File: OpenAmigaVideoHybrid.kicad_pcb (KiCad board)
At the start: 2 copper layers, 56.4 x 21.1 mm, 52 parts, among them J1 Conn_01x22, J99 OSHW_LOGO, Q1 2N3904, Q2 2N3904, Q3 2N3904, Q4 2N3904, Q5 2N3904, Q6 2N3906

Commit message: work in progress
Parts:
- removed J99: OSHW_LOGO, w_logo:Logo_copper_OSHW_6x6mm
- added C6: 100n, Capacitor_SMD:C_0603_1608Metric, F.Cu at (102.9, 91.9)
- added JP1: VCC_VID_BRIDGE, Jumper:SolderJumper-2_P1.3mm_Open_RoundedPad1.0x1.5mm, F.Cu at (162.8, 94.0)
- added R40: 2k, Resistor_SMD:R_0603_1608Metric, F.Cu at (151.8, 95.0)
- added R41: 2k, Resistor_SMD:R_0603_1608Metric, F.Cu at (139.1, 95.0)
- added R42: 2k, Resistor_SMD:R_0603_1608Metric, F.Cu at (126.4, 95.0)
- added R43: 4k7, Resistor_SMD:R_0603_1608Metric, F.Cu at (123.8, 95.0)
- added R44: 4k7, Resistor_SMD:R_0603_1608Metric, F.Cu at (136.5, 95.0)
- added R45: 4k7, Resistor_SMD:R_0603_1608Metric, F.Cu at (149.2, 95.0)
- added R46: 1k5, Resistor_SMD:R_0603_1608Metric, F.Cu at (129.8, 91.9)
- added R47: 1k5, Resistor_SMD:R_0603_1608Metric, F.Cu at (118.0, 95.0)
- added R48: 470, Resistor_SMD:R_0603_1608Metric, F.Cu at (142.4, 91.9)
- added R49: 3k3, Resistor_SMD:R_0603_1608Metric, F.Cu at (155.1, 91.9)
- added R50: 4k7, Resistor_SMD:R_0603_1608Metric, F.Cu at (119.6, 95.0)
- C1, C2, C3, C4: footprint Capacitors_SMD:C_0805_HandSoldering -> Capacitor_SMD:C_0603_1608Metric; moved to F.Cu
- C5: footprint Capacitors_SMD:C_0805_HandSoldering -> Capacitor_SMD:C_0603_1608Metric
- J1: footprint OpenAmigaVideoHybrid:Pin_Header_Straight_1x22_Pitch2.54mm -> Connector_PinHeader_2.54mm:PinHeader_1x22_P2.54mm_Vertical; moved to F.Cu
- Q1, Q2, Q3, Q4: value 2N3904 -> MMBT3904; footprint OpenAmigaVideoHybrid:2N3904_2N3906_SOT-23 -> Package_TO_SOT_SMD:SOT-23; moved to F.Cu
- Q5: value 2N3904 -> MMBT3904; footprint OpenAmigaVideoHybrid:2N3904_2N3906_SOT-23 -> Package_TO_SOT_SMD:SOT-23
- Q6: value 2N3906 -> S9012; footprint OpenAmigaVideoHybrid:2N3904_2N3906_SOT-23 -> Package_TO_SOT_SMD:SOT-23
- R1, R10, R13, R14, R15, R16, R17, R18, R2, R21, R22, R23, R24, R25, R26, R27, R28, R29, R5, R6, R7, R8, R9: footprint Resistors_SMD:R_0805_HandSoldering -> Resistor_SMD:R_0603_1608Metric; moved to F.Cu
- R11, R19, R3: value 4k -> 2k; footprint Resistors_SMD:R_0805_HandSoldering -> Resistor_SMD:R_0603_1608Metric; moved to F.Cu
- R12, R20, R4: value 8k -> 3k3; footprint Resistors_SMD:R_0805_HandSoldering -> Resistor_SMD:R_0603_1608Metric; moved to F.Cu
- R30: value 90.9k -> 91k; footprint Resistors_SMD:R_0805_HandSoldering -> Resistor_SMD:R_0603_1608Metric
- R31, R34: value 37.4k -> 36k; footprint Resistors_SMD:R_0805_HandSoldering -> Resistor_SMD:R_0603_1608Metric
- R32: value 13.3k -> 10k; footprint Resistors_SMD:R_0805_HandSoldering -> Resistor_SMD:R_0603_1608Metric
- R33: value 6.04k -> 5k6; footprint Resistors_SMD:R_0805_HandSoldering -> Resistor_SMD:R_0603_1608Metric
- R35: value 19.6k -> 15k; footprint Resistors_SMD:R_0805_HandSoldering -> Resistor_SMD:R_0603_1608Metric
- R36: value 220 -> 270; footprint Resistors_SMD:R_0805_HandSoldering -> Resistor_SMD:R_0603_1608Metric
- R37, R38: value 36 -> 33; footprint Resistors_SMD:R_0805_HandSoldering -> Resistor_SMD:R_0603_1608Metric
- R39: footprint Resistors_SMD:R_0805_HandSoldering -> Resistor_SMD:R_0603_1608Metric
- moved R27 64.2 mm to (104.9, 95.1), turned to -90 degrees
- moved Q4 63.7 mm to (107.8, 91.4), turned to 90 degrees
- moved C4 63.7 mm to (102.9, 95.0), turned to 90 degrees
- moved R28 62.2 mm to (107.4, 95.0)
- moved R25 61.1 mm to (104.9, 91.9)
- moved R29 60.9 mm to (110.2, 98.0)
- moved Q6 59.8 mm to (113.3, 91.4)
- moved R39 58.6 mm to (112.0, 98.0), turned to 90 degrees
- moved C5 56.3 mm to (112.0, 95.0)
- moved R37 55.4 mm to (114.3, 95.0), turned to 90 degrees
- moved R38 54.8 mm to (116.1, 95.0), turned to -90 degrees
- moved R26 52.4 mm to (114.3, 98.0)
- moved R36 51.1 mm to (113.2, 88.6), turned to 0 degrees
- moved Q5 49.4 mm to (117.0, 91.4), turned to -90 degrees
- moved R31 49.0 mm to (118.0, 98.0)
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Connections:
- J1 pad 2: VCC -> VID
- Q1 pad 1: Net-(Q1-Pad1) -> Net-(Q1-B)
- Q1 pad 2: Net-(Q1-Pad2) -> Net-(Q1-E)
- Q2 pad 1: Net-(Q2-Pad1) -> Net-(Q2-B)
- Q2 pad 2: Net-(Q2-Pad2) -> Net-(Q2-E)
- Q3 pad 1: Net-(Q3-Pad1) -> Net-(Q3-B)
- Q3 pad 2: Net-(Q3-Pad2) -> Net-(Q3-E)
- Q4 pad 1: Net-(Q4-Pad1) -> Net-(Q4-B)
- Q4 pad 2: Net-(Q4-Pad2) -> Net-(Q4-E)
- Q5 pad 1: Net-(Q5-Pad1) -> Net-(Q5-B)
- Q5 pad 2: Net-(Q5-Pad2) -> Net-(Q5-E)
- Q5 pad 3: Net-(Q5-Pad3) -> Net-(Q5-C)
- Q6 pad 1: VCC -> Net-(Q5-C)
- Q6 pad 2: Net-(Q5-Pad3) -> VCC
- R1 pad 1: Net-(Q1-Pad2) -> Net-(Q1-B)
- R10 pad 1: Net-(Q2-Pad2) -> Net-(Q2-B)
- R11 pad 1: Net-(Q2-Pad2) -> Net-(R11-Pad1)
- R12 pad 1: Net-(Q2-Pad2) -> Net-(R12-Pad1)
- R13 pad 1: VCC -> VID
- R13 pad 2: Net-(Q2-Pad2) -> Net-(Q2-B)
- R14 pad 1: Net-(Q2-Pad2) -> Net-(Q2-B)
- R15 pad 1: Net-(Q2-Pad1) -> Net-(Q2-E)
- R16 pad 2: Net-(Q2-Pad1) -> Net-(Q2-E)
- R17 pad 1: Net-(Q3-Pad2) -> Net-(Q3-B)
- R18 pad 1: Net-(Q3-Pad2) -> Net-(Q3-B)
- R19 pad 1: Net-(Q3-Pad2) -> Net-(R19-Pad1)
- R2 pad 1: Net-(Q1-Pad2) -> Net-(Q1-B)
- R20 pad 1: Net-(Q3-Pad2) -> Net-(R20-Pad1)
- R21 pad 1: VCC -> VID
- R21 pad 2: Net-(Q3-Pad2) -> Net-(Q3-B)
- R22 pad 1: Net-(Q3-Pad2) -> Net-(Q3-B)
- R23 pad 1: Net-(Q3-Pad1) -> Net-(Q3-E)
- R24 pad 2: Net-(Q3-Pad1) -> Net-(Q3-E)
- R25 pad 1: VCC -> VID
- R25 pad 2: Net-(Q4-Pad2) -> Net-(Q4-B)
- R26 pad 1: Net-(Q4-Pad2) -> Net-(Q4-B)
- R27 pad 1: Net-(Q4-Pad2) -> Net-(Q4-B)
- R28 pad 1: Net-(Q4-Pad1) -> Net-(Q4-E)
- R29 pad 2: Net-(Q4-Pad1) -> Net-(Q4-E)
- R3 pad 1: Net-(Q1-Pad2) -> Net-(R3-Pad1)
- R30 pad 1: VCC -> VID
- R30 pad 2: Net-(Q5-Pad2) -> Net-(Q5-B)
- R31 pad 1: Net-(Q5-Pad2) -> Net-(R31-Pad1)
- R32 pad 1: Net-(Q5-Pad2) -> Net-(R32-Pad1)
- R32 pad 2: Net-(Q1-Pad2) -> Net-(Q1-B)
- R33 pad 1: Net-(Q5-Pad2) -> Net-(R33-Pad1)
- R33 pad 2: Net-(Q2-Pad2) -> Net-(Q2-B)
- R34 pad 1: Net-(Q5-Pad2) -> Net-(R34-Pad1)
- R34 pad 2: Net-(Q3-Pad2) -> Net-(Q3-B)
- R35 pad 1: Net-(Q5-Pad2) -> Net-(R35-Pad1)
- R36 pad 2: Net-(Q5-Pad3) -> Net-(Q5-C)
- R37 pad 2: Net-(Q5-Pad1) -> Net-(Q5-E)
- R38 pad 1: Net-(Q5-Pad1) -> Net-(Q5-E)
- R4 pad 1: Net-(Q1-Pad2) -> Net-(R4-Pad1)
- R5 pad 1: VCC -> VID
- R5 pad 2: Net-(Q1-Pad2) -> Net-(Q1-B)
- R6 pad 1: Net-(Q1-Pad2) -> Net-(Q1-B)
- R7 pad 1: Net-(Q1-Pad1) -> Net-(Q1-E)
- R8 pad 2: Net-(Q1-Pad1) -> Net-(Q1-E)
- R9 pad 1: Net-(Q2-Pad2) -> Net-(Q2-B)
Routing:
- net GND: track 160.8 -> 12.3 mm, vias 26 -> 9
- net VCC: track 159.2 -> 22.2 mm, vias 0 -> 4
- net Net-(Q5-B): track 0.00 -> 49.8 mm
- net Net-(Q5-Pad2): track 36.1 -> 0.00 mm
- net Net-(Q3-Pad2): track 30.5 -> 0.00 mm, vias 1 -> 0
- net Net-(Q1-Pad2): track 26.2 -> 0.00 mm, vias 1 -> 0
- net Net-(Q2-Pad2): track 25.7 -> 0.00 mm, vias 1 -> 0
- net Net-(Q1-B): track 0.00 -> 21.4 mm
- net Net-(Q2-B): track 0.00 -> 21.4 mm
- net Net-(Q5-Pad3): track 20.6 -> 0.00 mm
- net Net-(Q3-B): track 0.00 -> 20.1 mm
- net Net-(Q4-B): track 0.00 -> 16.0 mm
- net Net-(Q4-Pad2): track 15.1 -> 0.00 mm
- net Net-(Q4-Pad1): track 10.8 -> 0.00 mm
- net /csync: track 9.24 -> 0.00 mm
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- removed copper zone on B.Cu, net GND
- removed copper zone on F.Cu, net GND
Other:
- board size 56.4 x 21.1 mm -> 65 x 16 mm
- net class Default removed
- net class Power removed
- board text added: "390229-04"
- board text added: "OpenAmigaVideoHybrid"
- board text removed: "V1"
- board text removed: "github.com/SukkoPera/OpenAmigaVideoHybrid"

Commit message: work done
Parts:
- J1: footprint Connector_PinHeader_2.54mm:PinHeader_1x22_P2.54mm_Vertical -> OpenAmigaVideoHybrid:side_connector
- moved JP1 61.4 mm to (101.6, 98.8), turned to -90 degrees
- moved J1 26.8 mm to (132.0, 101.9), turned to 180 degrees
- moved C4 6.25 mm to (108.3, 91.9), turned to -90 degrees
- moved R36 4.41 mm to (110.4, 91.9), turned to 90 degrees
- moved R15 3.47 mm to (134.9, 95.0), turned to 90 degrees
- moved R7 3.47 mm to (147.6, 95.0), turned to 90 degrees
- moved R23 3.44 mm to (122.2, 95.0), turned to 90 degrees
- moved C2 2.87 mm to (136.5, 91.9), turned to -90 degrees
- moved C1 2.87 mm to (149.2, 91.9), turned to -90 degrees
- moved C3 2.81 mm to (123.8, 91.9), turned to -90 degrees
- moved Q4 2.03 mm to (105.8, 91.4)
- moved R27 1.65 mm to (103.3, 95.0)
- moved R25 1.65 mm to (103.3, 91.9)
- moved C6 1.27 mm to (101.6, 91.9)
- moved R28 0.89 mm to (106.6, 95.0)
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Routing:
- net VID: track 3.16 -> 89.6 mm, vias 1 -> 0
- net VCC: track 22.2 -> 103.4 mm, vias 4 -> 5
- net GND: track 12.3 -> 28.3 mm, vias 9 -> 14
- net Net-(Q5-B): track 49.8 -> 58.5 mm
- net /csync: track 0.00 -> 6.65 mm
- net /red: track 0.00 -> 5.71 mm
- net Net-(Q5-C): track 8.08 -> 12.3 mm
- net Net-(Q3-E): track 8.73 -> 11.6 mm
- net Net-(Q2-E): track 8.73 -> 11.4 mm
- net Net-(Q1-E): track 8.73 -> 11.2 mm
- net Net-(Q4-E): track 6.55 -> 8.13 mm
- net Net-(R31-Pad1): track 0.00 -> 1.40 mm
- net Net-(Q4-B): track 16.0 -> 17.3 mm
- net Net-(Q1-B): track 21.4 -> 20.2 mm
- net Net-(Q2-B): track 21.4 -> 20.4 mm
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- added copper zone on B.Cu, net GND
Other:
- outline, holes or cut-outs redrawn

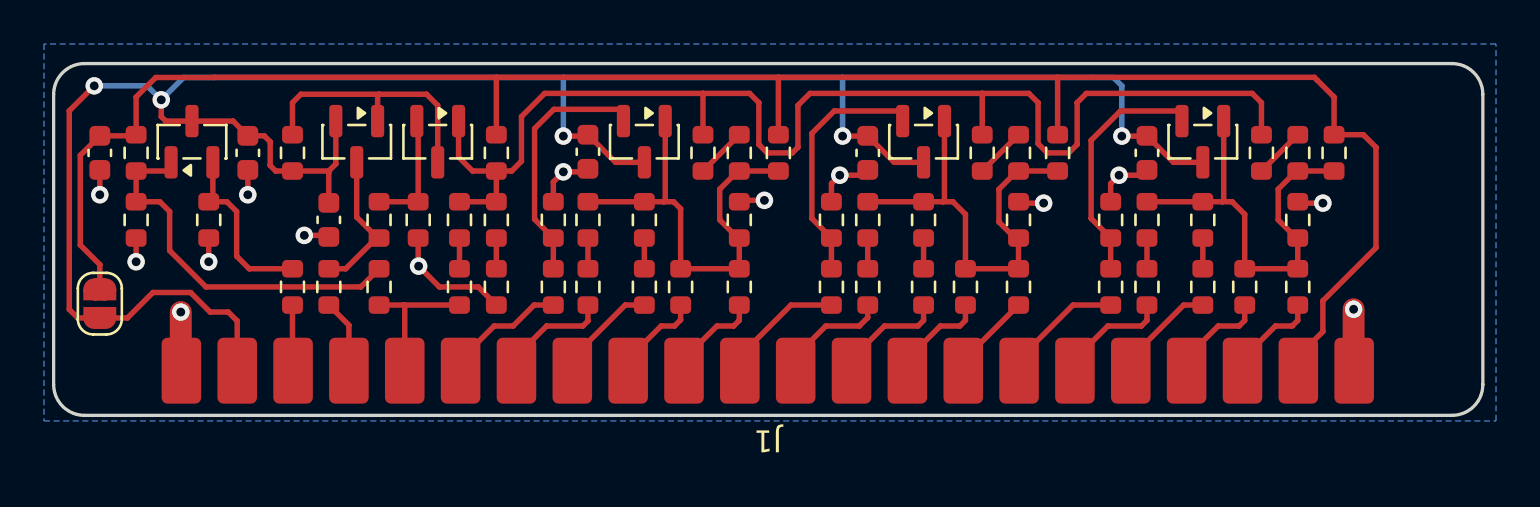
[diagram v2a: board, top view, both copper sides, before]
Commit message: routing done
DRC pass
added fiducials and silkscreen
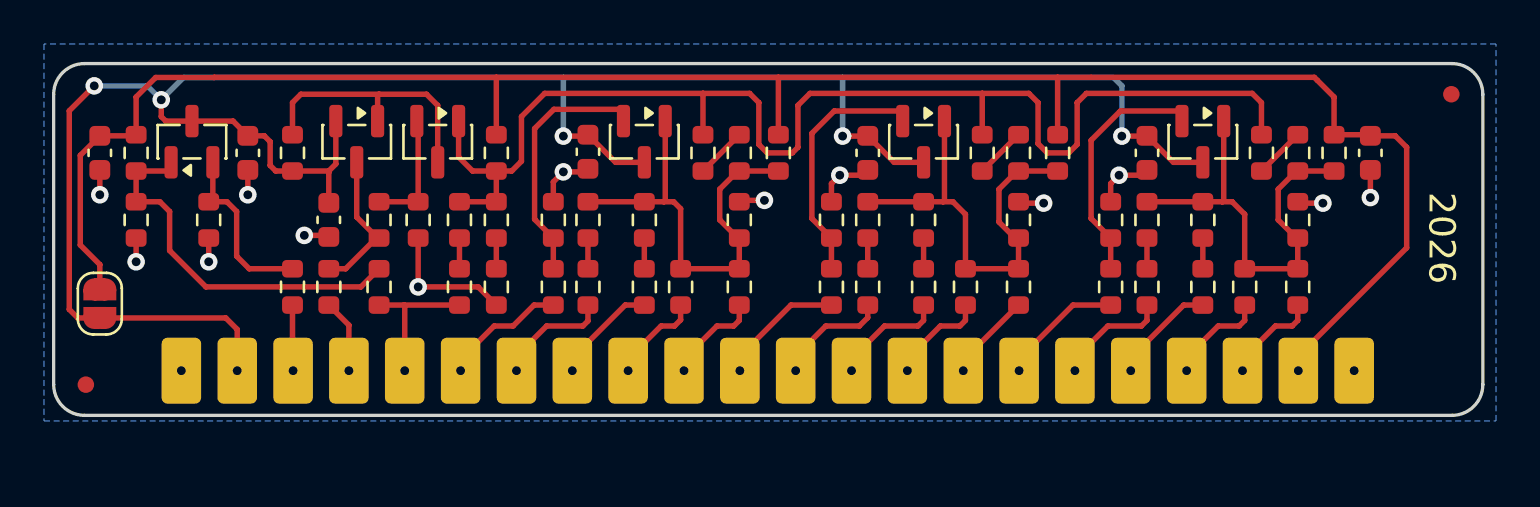
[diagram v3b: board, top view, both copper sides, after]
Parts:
- added C7: 100n, Capacitor_SMD:C_0603_1608Metric, F.Cu at (159.4, 91.9)
- added REF1: Fiducial_0.75mm_Mask1.5mm, Fiducial:Fiducial_0.75mm_Mask1.5mm, F.Cu at (101.0, 102.5)
- added REF2: Fiducial_0.75mm_Mask1.5mm, Fiducial:Fiducial_0.75mm_Mask1.5mm, F.Cu at (163.1, 89.3)
- added REF3: OSHW-Symbol_6.7x6mm_SilkScreen, Symbol:OSHW-Symbol_6.7x6mm_SilkScreen, B.Cu at (106.9, 96.3)
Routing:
- net GND: track 28.3 -> 24.6 mm, vias 14 -> 13
- net VID: track 89.6 -> 91.6 mm
- net VCC: track 103.4 -> 102.2 mm
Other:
- board text added: "2026"
- board text added: "DvW/SukkuPerra"
- board text added: "OpenAmigaVideoHybrid-4"
- board text removed: "390229-04"
- board text removed: "OpenAmigaVideoHybrid"

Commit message: designators renumbered
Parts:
- renumbered C7 to C1, C6 to C2, C1 to C3, C2 to C4, C3 to C5, C4 to C6, C5 to C7, Q5 to Q4, Q4 to Q5, R18 to R10, R19 to R11, R20 to R12, R40 to R13, R45 to R14, R41 to R15, R44 to R16, R42 to R17, R43 to R18, R5 to R19, R6 to R20, R13 to R21, R14 to R22, R21 to R23, R22 to R24, R7 to R25, R15 to R26, R23 to R27, R8 to R28, R16 to R29, R24 to R30, R47 to R35, R49 to R36, R48 to R37, R46 to R38, R30 to R39, R50 to R40, R35 to R41, R26 to R42, R25 to R43, R27 to R44, R36 to R45, R28 to R46, R37 to R47, R38 to R48, R29 to R49, R9 to R5, R39 to R50, R10 to R6, R11 to R7, R12 to R8, R17 to R9

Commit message: updated BOM for assembly by JLCPCB
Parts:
- moved REF3 0.13 mm to (106.9, 96.4)
